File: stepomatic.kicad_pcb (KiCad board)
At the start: 2 copper layers, 50 x 30 mm, 86 parts, among them J1 I2C, J2 5V Switch, J4 USB_B_Micro, Q1 MMBT3904, Q2 MMBT3904, SW1 Mode, SW2 RST, U1 HDC1080DMBR, U3 ULN2003A, U4 CH340C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

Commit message: SK6812-HS
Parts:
- removed D1: WS2812B, footprint:LED-SMD_4P-L5.0-W5.0-BL_XL-5050RGBC
- added U2: SK6812MINI-HS Neopixel, footprint:LED-SMD_4P-L3.5-W3.5-BR_SK6812MINI-HS, F.Cu at (121.8, 89.5)
- moved TP8 1.76 mm to (124.7, 88.6)
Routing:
- net NEOPIXEL: track 33.3 -> 26.1 mm, vias 4 -> 2
- net RX: track 32.6 -> 30.4 mm
- net RESET: track 62.2 -> 60.6 mm
- net I2C_SDA: track 42.6 -> 44.1 mm, vias 2 -> 4
- net NEOPIXEL_OUT: track 2.05 -> 3.01 mm
- net GND: track 50.5 -> 51.2 mm
- net STEPPER4: track 20.9 -> 20.4 mm

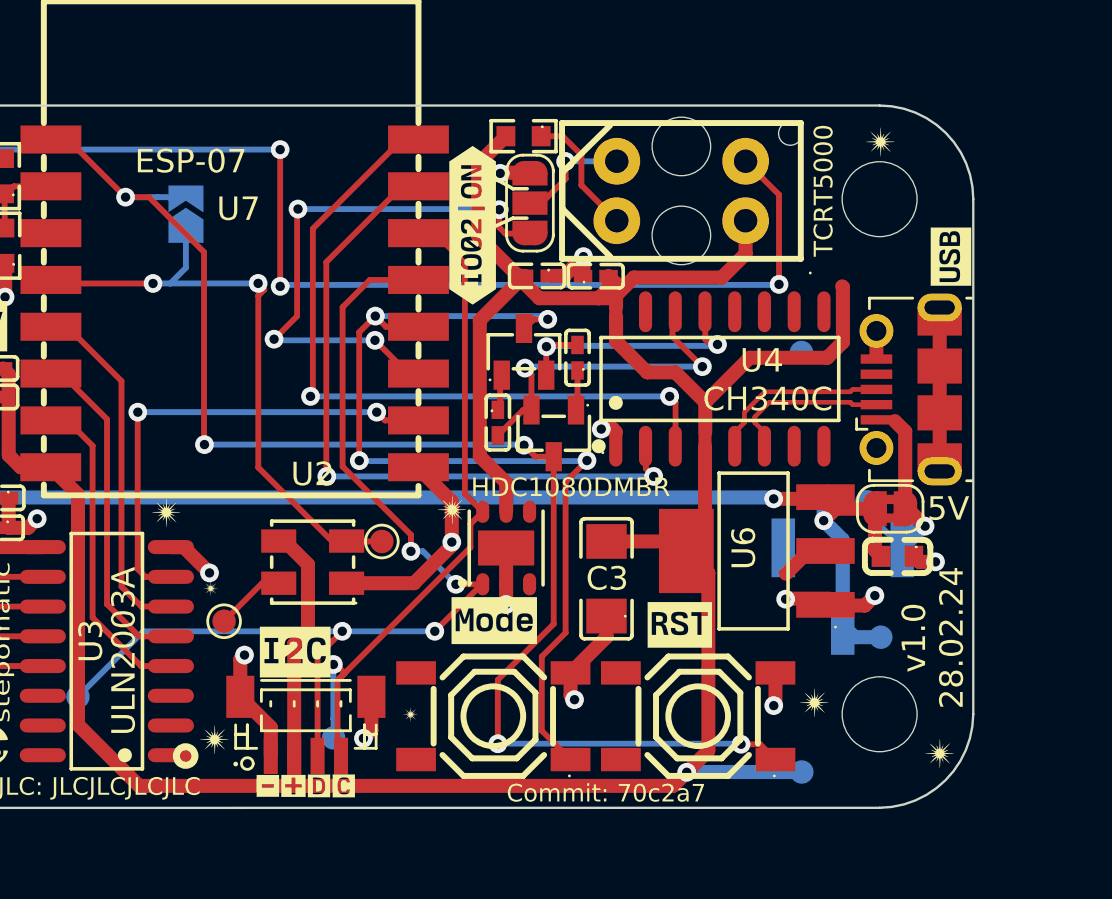
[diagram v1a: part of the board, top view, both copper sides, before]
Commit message: Make IO2 the default for the TCRT5000
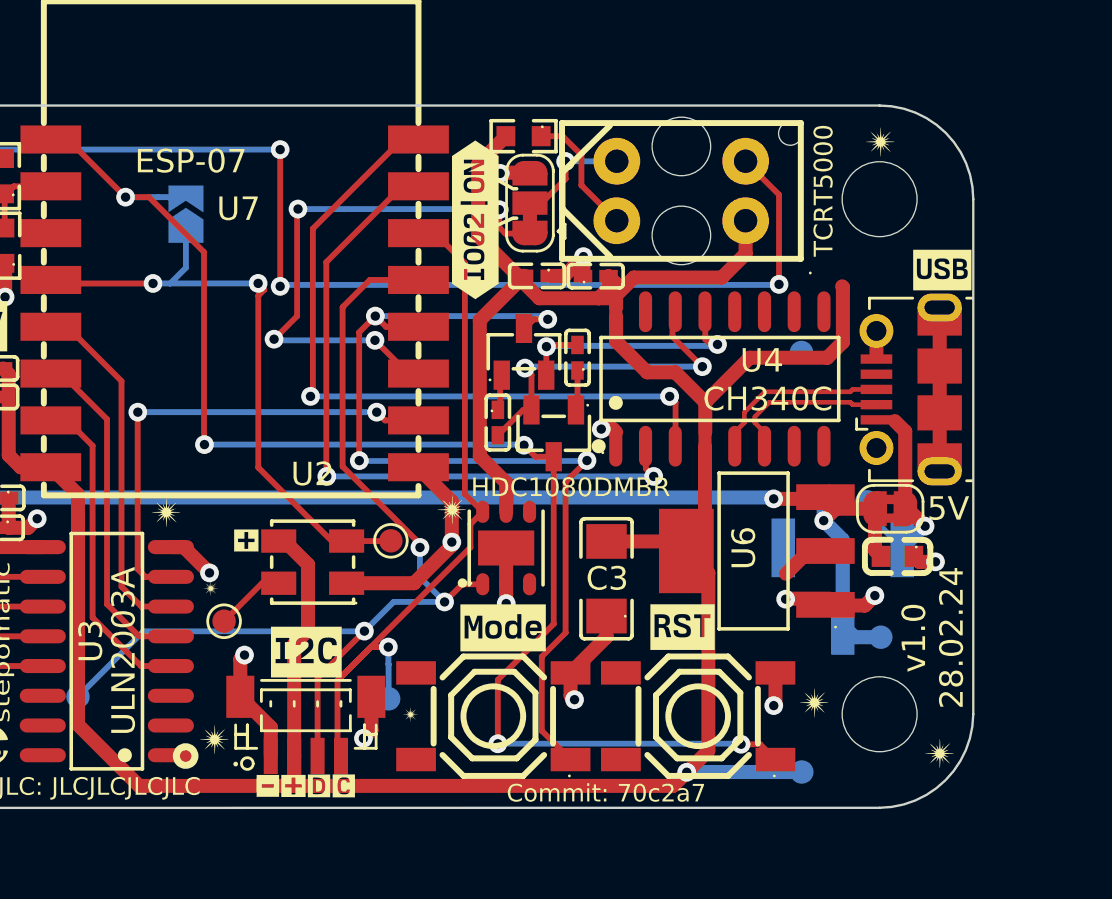
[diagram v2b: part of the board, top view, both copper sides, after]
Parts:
- added kibuzzard-65DB2C93: G***, kibuzzard-65DB2C93, F.Cu at (118.9, 88.6)
- JPe: renamed from JP2; footprint Jumper:SolderJumper-3_P1.3mm_Open_RoundedPad1.0x1.5mm -> Jumper:SolderJumper-3_P1.3mm_Bridged12_RoundedPad1.0x1.5mm
- moved TP1 2.89 mm to (125.0, 95.3)
- moved kibuzzard-65D87D0C 0.68 mm to (148.7, 77.0), turned to 0 degrees
- moved kibuzzard-65D87D4C 0.49 mm to (129.9, 92.3)
- moved kibuzzard-65D87D58 0.48 mm to (121.5, 93.3)
- moved TP8 0.39 mm to (125.1, 88.6)
- moved kibuzzard-65DB2D65 0.26 mm to (128.7, 74.9)
- moved kibuzzard-65D87D42 0.15 mm to (137.6, 92.3)
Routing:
- net I2C_SCL: track 30.7 -> 31.5 mm
- net I2C_SDA: track 44.1 -> 43.6 mm, vias 4 -> 3

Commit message: Update version
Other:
- board text added: "Commit: eed668"
- board text added: "v1.0 01.03.24"
- board text removed: "Commit: 70c2a7"
- board text removed: "v1.0 28.02.24"
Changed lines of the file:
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@@
   (gr_line (start 130.392555 73.554657) (end 130.5 73.554657)
     (stroke (width 0.15) (type solid)) (layer "F.SilkS"))
+  (gr_circle (center 124 91) (end 124.087099 91.042728)
+    (stroke (width 0.15) (type default)) (fill none) (layer "F.SilkS"))
   (gr_line (start 129.607582 75.144388) (end 130.335286 74.81083)
     (stroke (width 0.15) (type solid)) (layer "F.SilkS"))
@@
   (gr_arc (start 146 70) (mid 148.828427 71.171573) (end 150 74)
     (stroke (width 0.1) (type solid)) (layer "Edge.Cuts"))
-  (gr_text "v1.0\n28.02.24" (at 148.282479 92.73096 90) (layer "F.SilkS")
+  (gr_text "v1.0\n01.03.24" (at 148.282479 92.73096 90) (layer "F.SilkS")
     (effects (font (size 1 1) (thickness 0.1)))
   )
-  (gr_text "Commit: 70c2a7" (at 130.060288 99.378202) (layer "F.SilkS")
+  (gr_text "Commit: eed668" (at 130.060288 99.378202) (layer "F.SilkS")
     (effects (font (size 0.75 0.75) (thickness 0.1)) (justify left))
   )

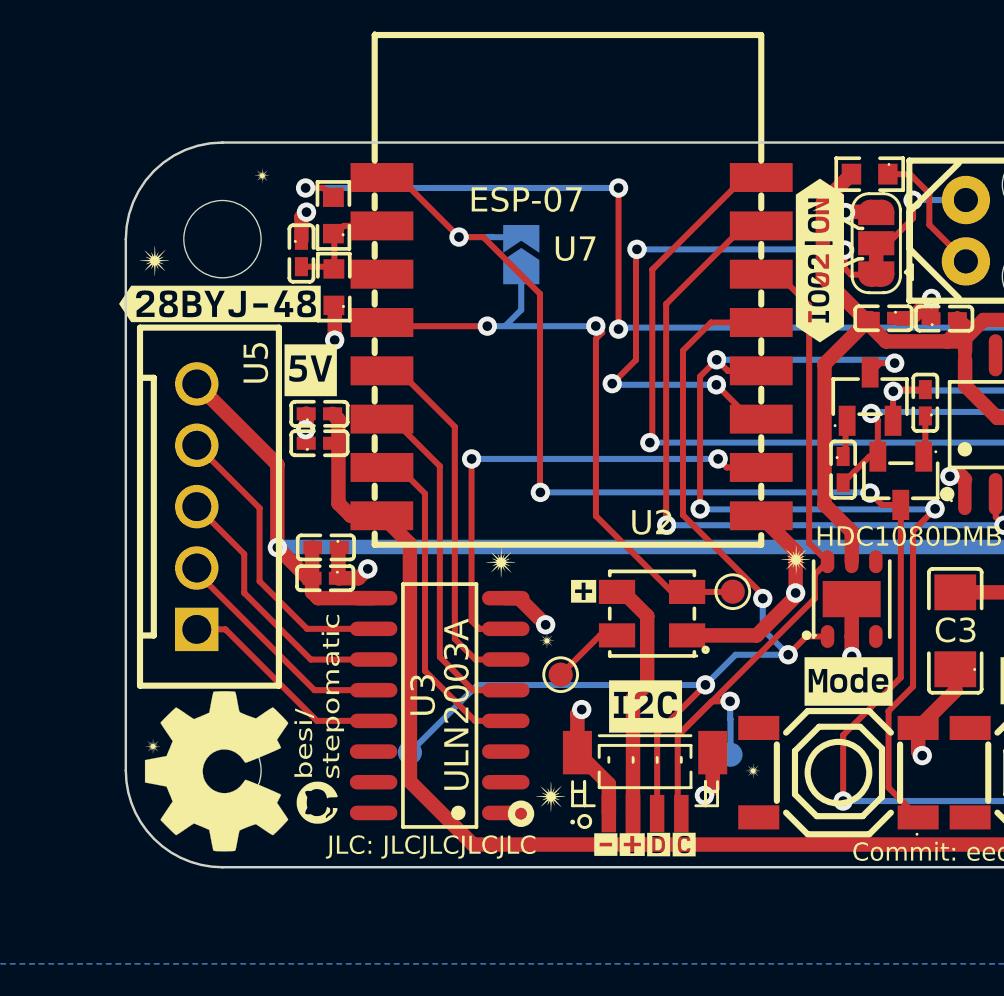
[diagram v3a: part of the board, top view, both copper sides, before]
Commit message: Last twaks
Add a jumper to disable the Neopixel
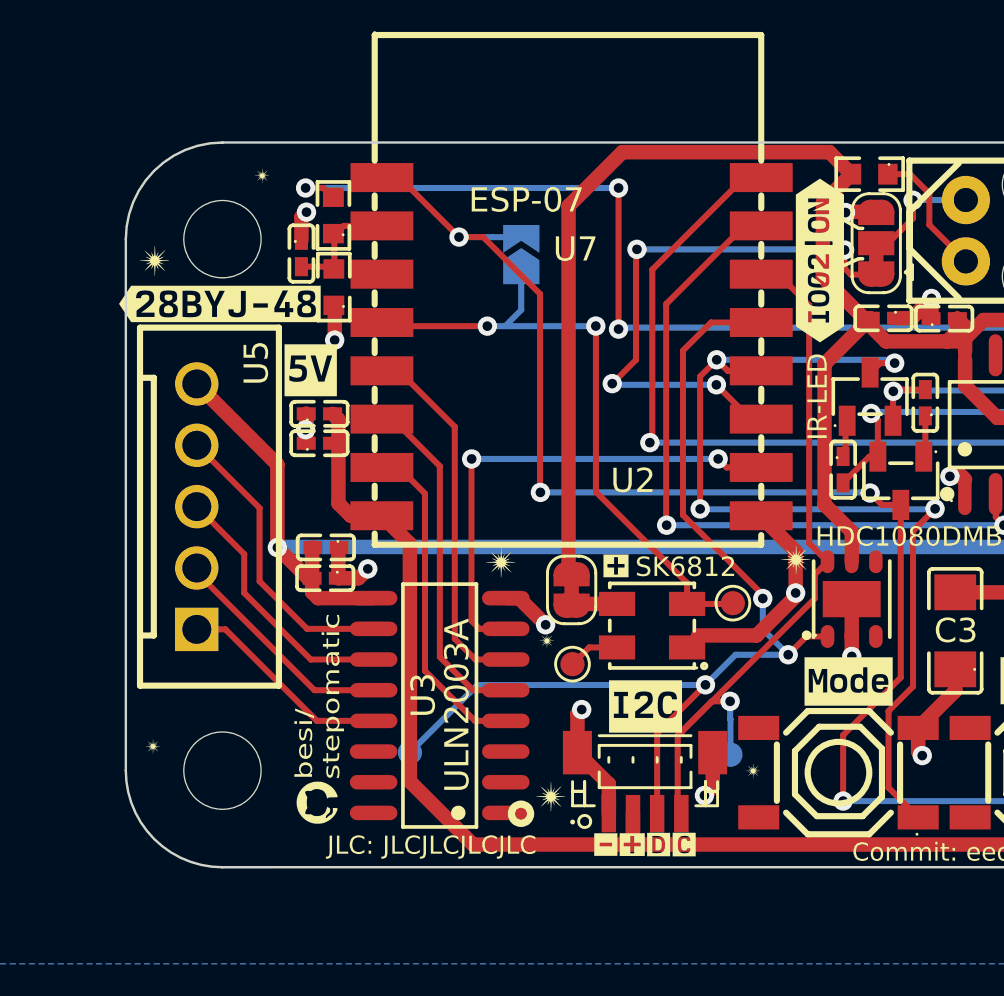
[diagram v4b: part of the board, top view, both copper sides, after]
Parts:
- removed REF**: OSHW-Symbol_6.7x6mm_SilkScreen, Symbol:OSHW-Symbol_6.7x6mm_SilkScreen
- added JPe: Enable Neopixel, Jumper:SolderJumper-2_P1.3mm_Bridged_RoundedPad1.0x1.5mm, F.Cu at (118.5, 88.5)
- JP2: renamed from JPe; value IR -> IR-LED
- U2: value SK6812MINI-HS Neopixel -> SK6812
- moved kibuzzard-65DB2C93 1.71 mm to (120.3, 87.5)
- moved TP7 0.65 mm to (118.5, 91.6)
- moved U2 0.50 mm to (121.8, 90.0)
- moved TP8 0.47 mm to (125.1, 89.1)
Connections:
- U2 pad 3: +3V3 -> Net-(JP4-B)
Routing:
- net +3V3: track 132.3 -> 150.5 mm
- net Net-(JP4-B): track 0.00 -> 1.91 mm
- net NEOPIXEL_OUT: track 3.01 -> 2.13 mm

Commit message: JLC Order 7.03.2024
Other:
- board text added: "Commit: 2df132"
- board text added: "v1.0 07.03.24"
- board text removed: "Commit: eed668"
- board text removed: "v1.0 01.03.24"
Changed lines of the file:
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@@
   (gr_arc (start 146 70) (mid 148.828427 71.171573) (end 150 74)
     (stroke (width 0.1) (type solid)) (layer "Edge.Cuts"))
-  (gr_text "v1.0\n01.03.24" (at 148.282479 92.73096 90) (layer "F.SilkS")
+  (gr_text "v1.0\n07.03.24" (at 148.282479 92.73096 90) (layer "F.SilkS")
     (effects (font (size 1 1) (thickness 0.1)))
   )
-  (gr_text "Commit: eed668" (at 130.060288 99.378202) (layer "F.SilkS")
+  (gr_text "Commit: 2df132" (at 130.060288 99.378202) (layer "F.SilkS")
     (effects (font (size 0.75 0.75) (thickness 0.1)) (justify left))
   )

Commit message: Fix name of Jumper
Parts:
- renumbered JPe to JP4
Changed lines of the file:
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@@
     (attr exclude_from_pos_files)
     (net_tie_pad_groups "1, 2")
-    (fp_text reference "JPe" (at 0 -1.8 90) (layer "F.SilkS") hide
+    (fp_text reference "JP4" (at 0 -1.8 90) (layer "F.SilkS") hide
         (effects (font (size 1 1) (thickness 0.15)))
     )
@@
     (property "ki_keywords" "C2922787")
     (attr smd)
-    (fp_text reference "U2" (at -0.78349 -6) (layer "F.SilkS")
-        (effects (font (size 1 1) (thickness 0.15)))
-    )
+    (fp_text reference "U2" (at -0.01186 0.016312 90) (layer "F.SilkS")
+        (effects (font (size 1 1) (thickness 0.15)))
+    )

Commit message: Add OSHW Logo
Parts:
- added OSHW1: Logo_Open_Hardware_Small, Symbol:OSHW-Symbol_6.7x6mm_SilkScreen, F.Cu at (103.7, 96.0)
- U2: value SK6812 -> SK6812MINI-HS Neopixel

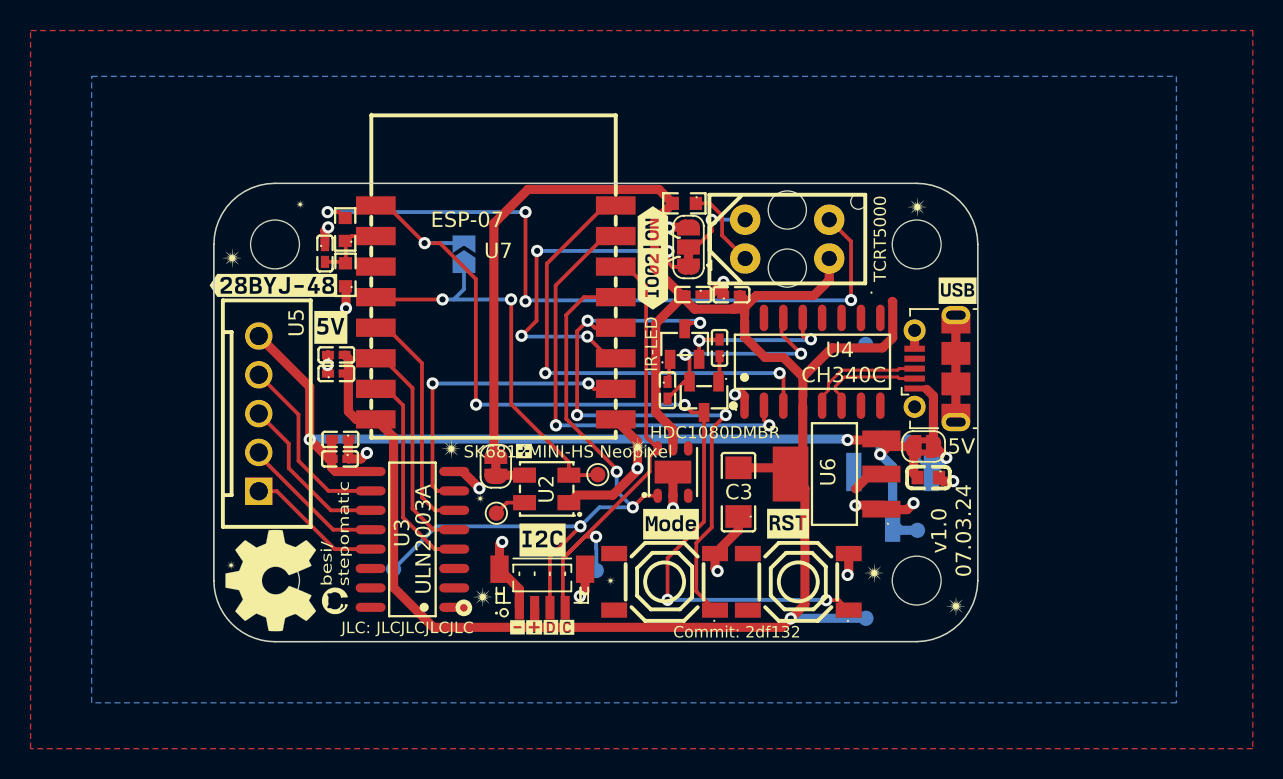
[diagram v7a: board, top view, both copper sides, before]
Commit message: More comprehensive 5V switch
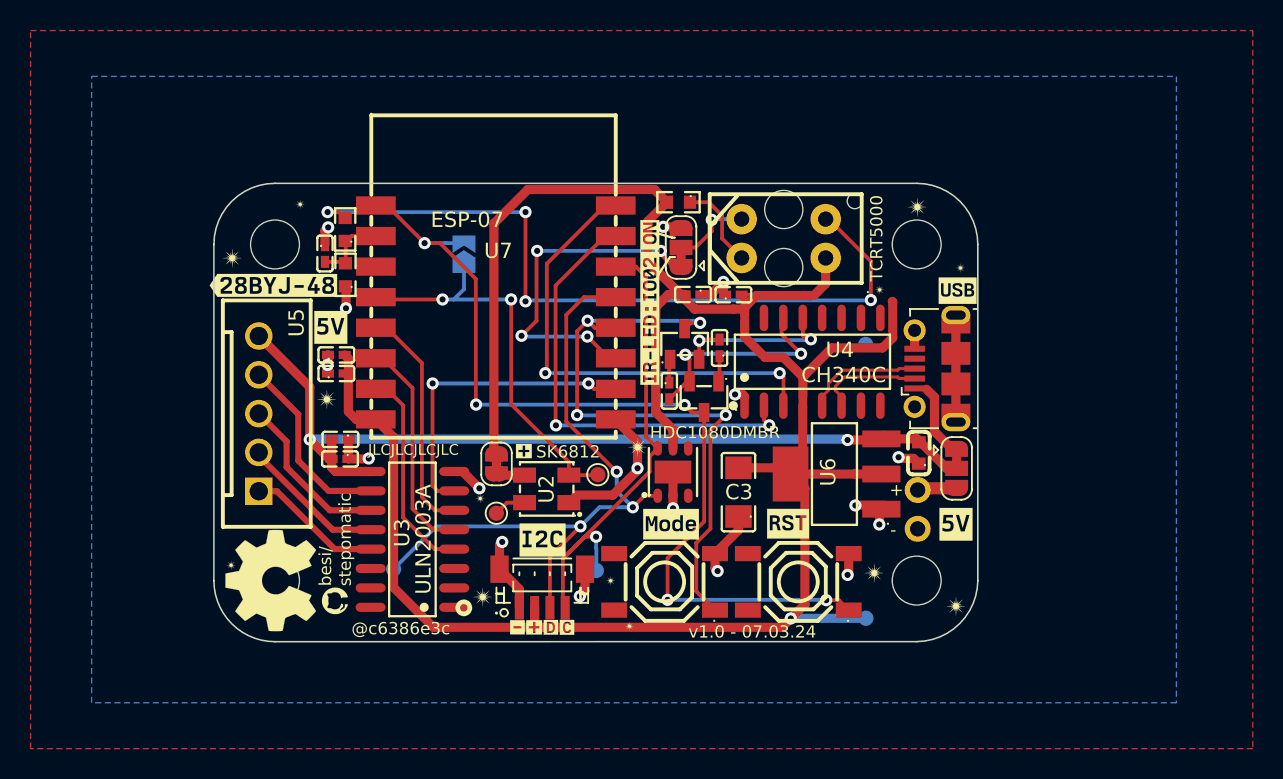
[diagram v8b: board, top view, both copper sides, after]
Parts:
- removed TP3, TP4: VBUS, TestPoint:TestPoint_Pad_D1.0mm
- removed kibuzzard-65DB2D65: G***, kibuzzard-65DB2D65
- added G***: LOGO, LOGO, F.Cu at (127.2, 99.0)
- added G***: LOGO, LOGO, B.Cu at (149.2, 81.3)
- added G***: LOGO, LOGO, B.Cu at (136.5, 73.7)
- added G***: LOGO, LOGO, F.Cu at (148.9, 75.5)
- added G***: LOGO, LOGO, B.Cu at (117.8, 70.7)
- added G***: LOGO, LOGO, F.Cu at (143.6, 77.0)
- added kibuzzard-65D87D77: G***, kibuzzard-65D87D77, F.Cu at (148.6, 92.3)
- added kibuzzard-65EA2F1C: G***, kibuzzard-65EA2F1C, F.Cu at (128.5, 77.8)
- J2: value 5V Switch -> 5V External; footprint Connector_PinHeader_2.54mm:PinHeader_1x03_P2.54mm_Vertical_SMD_Pin1Left -> Connector_PinHeader_2.54mm:PinHeader_1x02_P2.54mm_Horizontal
- JP3: value 5V -> 5V Switch; footprint Jumper:SolderJumper-2_P1.3mm_Bridged2Bar_RoundedPad1.0x1.5mm -> Jumper:SolderJumper-3_P1.3mm_Bridged12_RoundedPad1.0x1.5mm
- OSHW1: value Logo_Open_Hardware_Small -> github.com/besi/stepomatic
- U2: value SK6812MINI-HS Neopixel -> SK6812
- moved G*** 8.76 mm to (107.4, 84.1)
- moved J2 2.64 mm to (146.1, 92.6), turned to 0 degrees
- moved JP3 2.59 mm to (148.6, 88.7), turned to -90 degrees
- moved C2 1.72 mm to (146.1, 87.6), turned to 90 degrees
- moved JP2 0.49 mm to (130.6, 74.2)
- moved R4 0.39 mm to (130.4, 71.2)
- moved CGQ1 0.24 mm to (137.3, 73.6)
- moved JP4 0.16 mm to (118.5, 88.4)
- moved R2 0.13 mm to (129.8, 83.6)
- moved C1 0.12 mm to (134.0, 77.3)
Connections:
- J2 pad 2: +5V -> +5VD
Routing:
- net +5V: track 64.6 -> 58.4 mm, vias 3 -> 2
- net VBUS: track 9.03 -> 4.89 mm, vias 1 -> 0
- net +3V3: track 150.5 -> 154.4 mm
- net +5VD: track 0.00 -> 2.60 mm
- net Net-(CGQ1-E): track 47.4 -> 49.4 mm
- net GND: track 51.2 -> 50.1 mm
- net IR: track 23.5 -> 22.8 mm
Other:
- board text added: "+"
- board text added: "-"
- board text added: "@c6386e3c"
- board text added: "v1.0 - 07.03.24"
- board text removed: "Commit: 2df132"
- board text removed: "JLC:"
- board text removed: "v1.0 07.03.24"
